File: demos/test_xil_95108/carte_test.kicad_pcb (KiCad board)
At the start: 2 copper layers, 101.6 x 99.7 mm, 42 parts, among them J1 DB25, J2 DB9FEM, K1 CONN_3, P2 CONN_3, P3 CONN_2, P4 CONN_2X2, SW1 SW_PUSH, SW2 SW_PUSH, U1 TDA8702, U2 XC95108PC84, U3 LM7805, U4 74HC04, U5 RAM_32KO, U6 LM318N, X1 10MHz

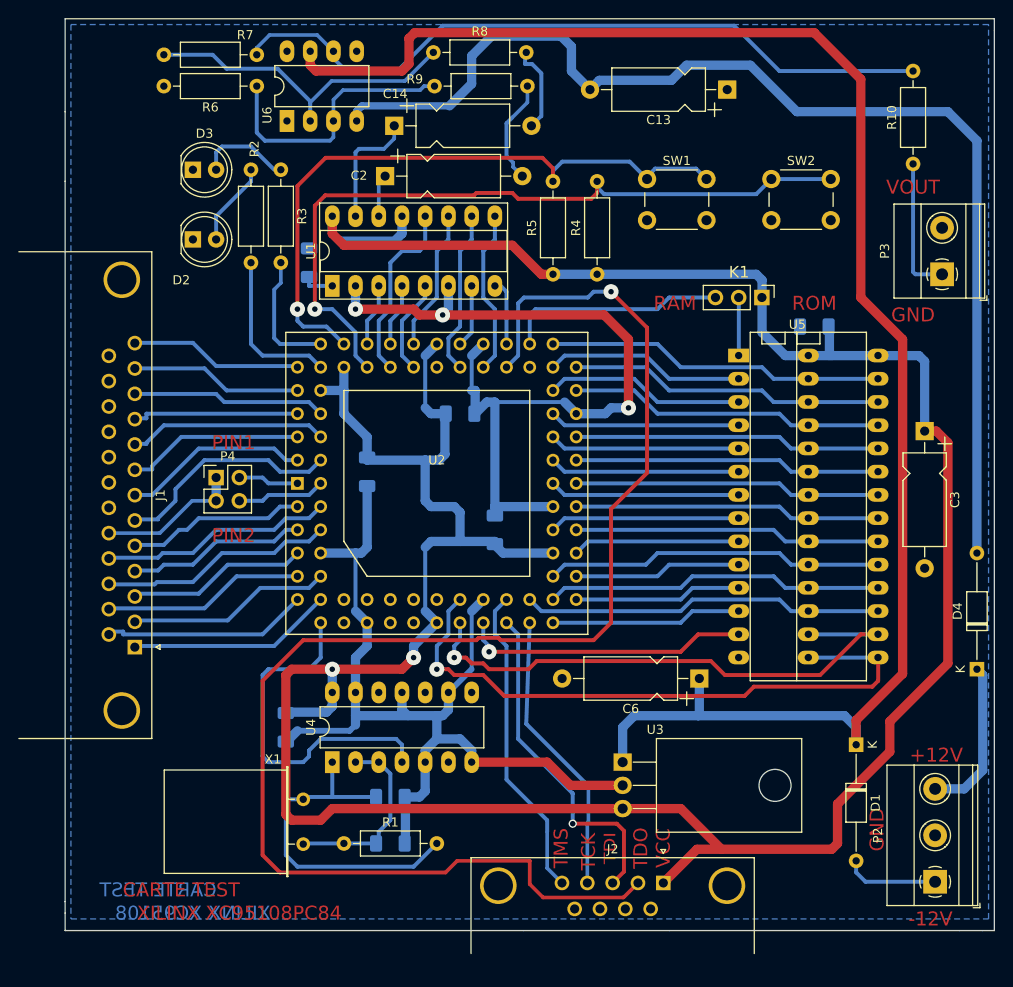
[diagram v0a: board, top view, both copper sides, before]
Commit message: feat: update kicad to 9.0.0+dfsg-1
Signed-off-by: lhdjply <lhdjply@126.com>
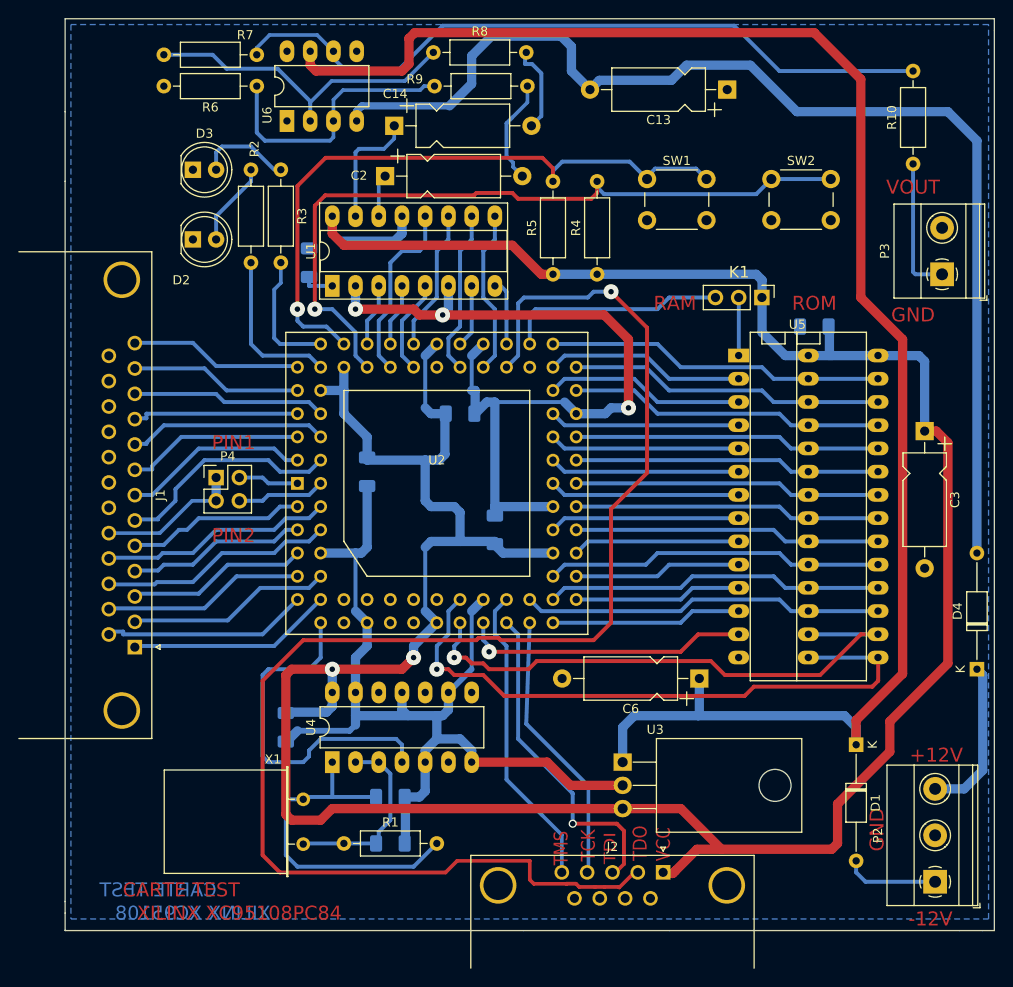
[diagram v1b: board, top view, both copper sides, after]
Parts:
- C1, C10, C11, C12, C4, C5, C7, C8: footprint Capacitor_SMD:C_1206_3216Metric_Pad1.33x1.80mm_HandSolder -> footprints:C_1206_3216Metric_Pad1.33x1.80mm_HandSolder
- C13, C14, C2, C3, C6: footprint Capacitor_THT:CP_Axial_L10.0mm_D4.5mm_P15.00mm_Horizontal -> footprints:CP_Axial_L10.0mm_D4.5mm_P15.00mm_Horizontal
- D1, D4: footprint Diode_THT:D_DO-35_SOD27_P12.70mm_Horizontal -> footprints:D_DO-35_SOD27_P12.70mm_Horizontal
- D2, D3: footprint LED_THT:LED_D5.0mm -> footprints:LED_D5.0mm
- J1: footprint Connector_Dsub:DSUB-25_Female_Horizontal_P2.77x2.84mm_EdgePinOffset9.90mm_Housed_MountingHolesOffset11.32mm -> footprints:DSUB-25_Female_Horizontal_P2.77x2.84mm_EdgePinOffset9.90mm_Housed_MountingHolesOffset11.32mm
- J2: footprint Connector_Dsub:DSUB-9_Female_Horizontal_P2.77x2.84mm_EdgePinOffset4.94mm_Housed_MountingHolesOffset7.48mm -> footprints:DSUB-9_Female_Horizontal_P2.77x2.84mm_EdgePinOffset7.70mm_Housed_MountingHolesOffset9.12mm
- K1: footprint Connector_PinHeader_2.54mm:PinHeader_1x03_P2.54mm_Vertical -> footprints:PinHeader_1x03_P2.54mm_Vertical
- P2: footprint TerminalBlock_Phoenix:TerminalBlock_Phoenix_MKDS-1,5-3-5.08_1x03_P5.08mm_Horizontal -> footprints:TerminalBlock_Phoenix_MKDS-1,5-3-5.08_1x03_P5.08mm_Horizontal
- P3: footprint TerminalBlock_Phoenix:TerminalBlock_Phoenix_MKDS-1,5-2-5.08_1x02_P5.08mm_Horizontal -> footprints:TerminalBlock_Phoenix_MKDS-1,5-2-5.08_1x02_P5.08mm_Horizontal
- P4: footprint Connector_PinHeader_2.54mm:PinHeader_2x02_P2.54mm_Vertical -> footprints:PinHeader_2x02_P2.54mm_Vertical
- R1, R10, R2, R3, R4, R5, R6, R7, R8, R9: footprint Resistor_THT:R_Axial_DIN0207_L6.3mm_D2.5mm_P10.16mm_Horizontal -> footprints:R_Axial_DIN0207_L6.3mm_D2.5mm_P10.16mm_Horizontal
- SW1, SW2: footprint Button_Switch_THT:SW_PUSH_6mm_H4.3mm -> footprints:SW_PUSH_6mm_H4.3mm
- U1: footprint Package_DIP:DIP-16_W7.62mm_Socket_LongPads -> footprints:DIP-16_W7.62mm_Socket_LongPads
- U3: footprint Package_TO_SOT_THT:TO-220-3_Horizontal_TabDown -> footprints:TO-220-3_Horizontal_TabDown
- U4: footprint Package_DIP:DIP-14_W7.62mm_LongPads -> footprints:DIP-14_W7.62mm_LongPads
- U6: footprint Package_DIP:DIP-8_W7.62mm_LongPads -> footprints:DIP-8_W7.62mm_LongPads
- X1: footprint Crystal:Crystal_HC18-U_Horizontal -> footprints:Crystal_HC18-U_Horizontal
- moved J2 1.16 mm to (160.0, 129.5)
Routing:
- net /TMS: track 34.6 -> 33.4 mm
- net /TCK: track 31.3 -> 30.2 mm
- net /TDI: track 37.1 -> 36.2 mm
- net /TDO: track 163.8 -> 163.1 mm
